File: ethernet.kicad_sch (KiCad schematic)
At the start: 1 part, among them U3 KSZ8081MLX

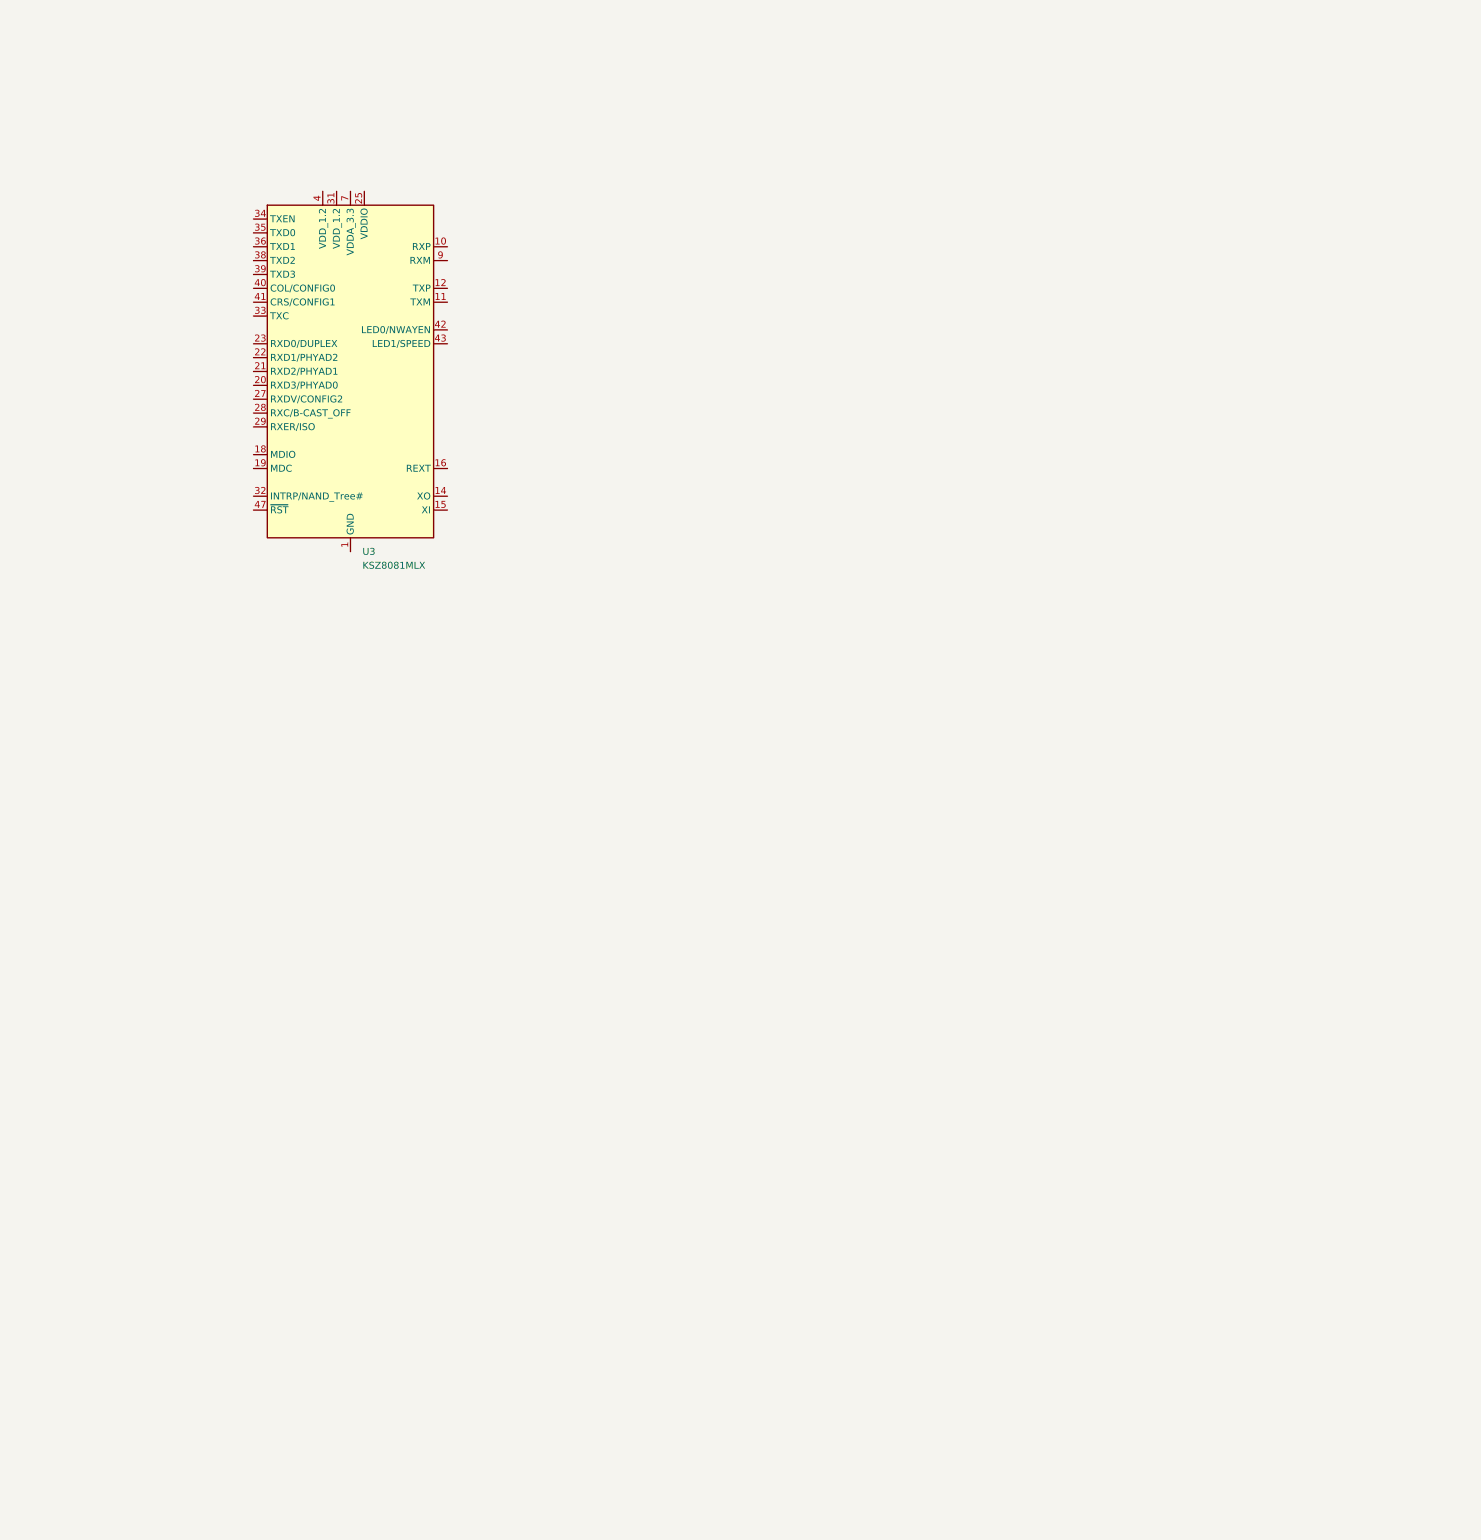
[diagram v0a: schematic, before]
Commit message: Working on ethernet schematic
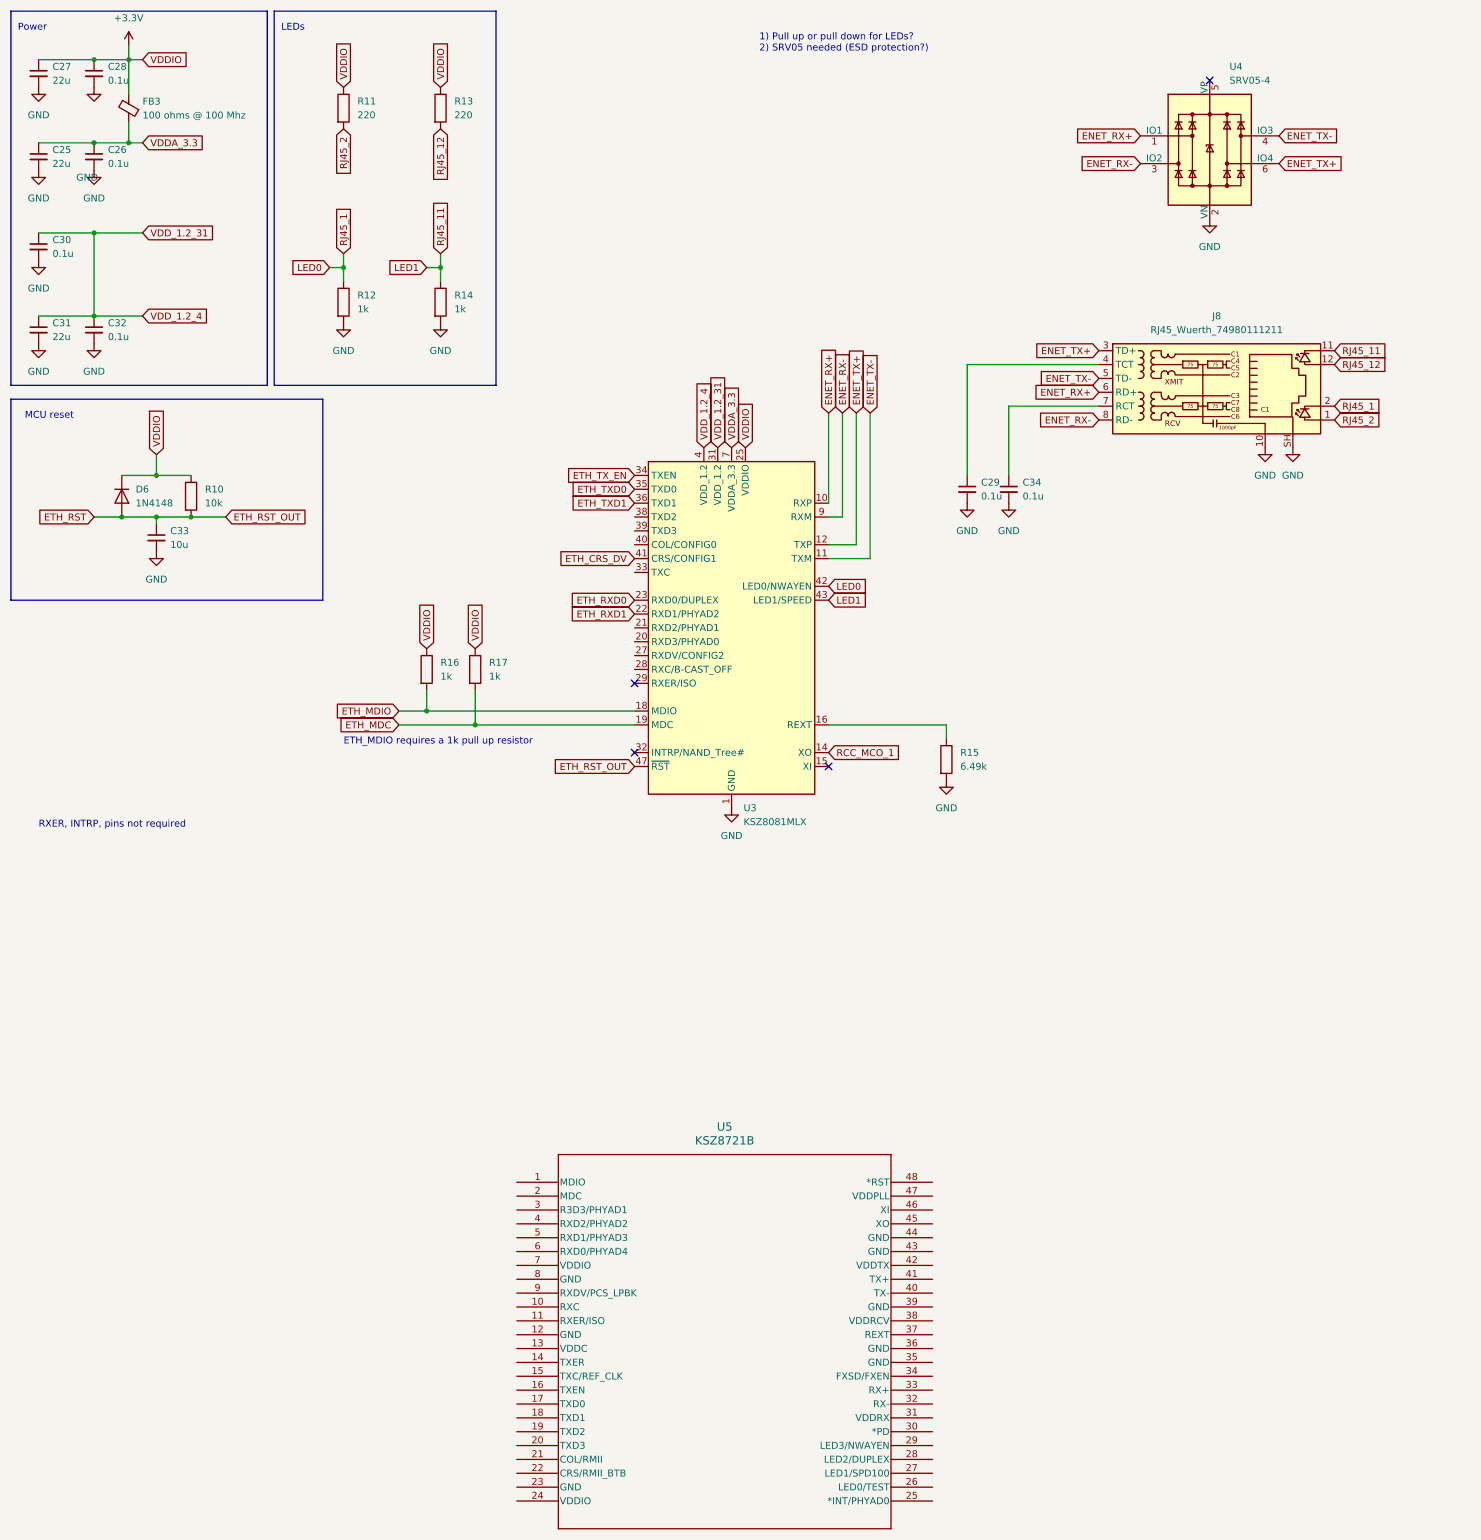
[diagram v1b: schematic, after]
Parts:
- added C25, C27, C31: 22u, symbol Device:C_Small
- added C26, C28, C29, C30, C32, C34: 0.1u, symbol Device:C_Small
- added C33: 10u, symbol Device:C_Small
- added D6: 1N4148, Diode_THT:D_DO-35_SOD27_P7.62mm_Horizontal, symbol Diode:1N4148
- added FB3: 100 ohms @ 100 Mhz, symbol Device:FerriteBead_Small
- added J8: RJ45_Wuerth_74980111211, Connector_RJ:RJ45_Wuerth_74980111211_Horizontal, symbol Connector:RJ45_Wuerth_74980111211
- added R10: 10k, symbol Device:R
- added R11, R13: 220, symbol Device:R
- added R12, R14, R16, R17: 1k, symbol Device:R
- added R15: 6.49k, symbol Device:R
- added U4: SRV05-4, Package_TO_SOT_SMD:SOT-23-6, symbol Power_Protection:SRV05-4
- added U5: KSZ8721B, SSOP48_15P875X7P493_MCH, symbol 2024-02-17_20-32-57:KSZ8721B
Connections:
- net GND: now reaches U3.1 (GND), U3.13 (GND), U3.17 (GND), U3.2 (GND), U3.24 (GND), U3.3 (GND), U3.30 (GND), U3.37 (GND)
- net GND: now also C25.2, C26.2, C27.2, C28.2, C29.2, C30.2, C31.2, C32.2, C33.2, C34.2, J8.10, J8.SH, R12.2, R14.2, R15.2, U4.2 (VN)
- net ENET_RX+: now reaches U3.10 (RXP)
- net ENET_RX+: now also J8.6 (RD+), U4.1 (IO1)
- net ENET_TX-: now reaches U3.11 (TXM)
- net ENET_TX-: now also J8.5 (TD-), U4.4 (IO3)
- net ENET_TX+: now reaches U3.12 (TXP)
- net ENET_TX+: now also J8.3 (TD+), U4.6 (IO4)
- net RCC_MCO_1: now reaches U3.14 (XO)
- net at U3.16 (REXT): now also R15.1
- net ETH_MDIO: now reaches U3.18 (MDIO)
- net ETH_MDIO: now also R16.2
- net ETH_MDC: now reaches U3.19 (MDC)
- net ETH_MDC: now also R17.2
- net ETH_RXD1: now reaches U3.22 (RXD1/PHYAD2)
- net ETH_RXD0: now reaches U3.23 (RXD0/DUPLEX)
- net +3.3V: now reaches U3.25 (VDDIO)
- net +3.3V: now also C27.1, C28.1, D6.1 (K), FB3.2, R10.1, R11.1, R13.1, R16.1, R17.1
- net VDD_1.2_31: now reaches U3.31 (VDD_1.2)
- net VDD_1.2_31: now also U3.4 (VDD_1.2), C30.1, C31.1, C32.1
- net ETH_TX_EN: now reaches U3.34 (TXEN)
- net ETH_TXD0: now reaches U3.35 (TXD0)
- net ETH_TXD1: now reaches U3.36 (TXD1)
- net ETH_CRS_DV: now reaches U3.41 (CRS/CONFIG1)
- net LED0: now reaches U3.42 (LED0/NWAYEN)
- net LED0: now also J8.2, R12.1
- net LED1: now reaches U3.43 (LED1/SPEED)
- net LED1: now also J8.11, R14.1
- net ETH_RST: now reaches U3.47 (~{RST})
- net ETH_RST: now also C33.1, D6.2 (A), R10.2
- net VDDA_3.3: now reaches U3.7 (VDDA_3.3)
- net VDDA_3.3: now also C25.1, C26.1, FB3.1
- net ENET_RX-: now reaches U3.9 (RXM)
- net ENET_RX-: now also J8.8 (RD-), U4.3 (IO2)
- new net: C29.1, J8.4 (TCT)
- new net: C34.1, J8.7 (RCT)
- new net RJ45_12: J8.12, R13.2
- new net RJ45_2: J8.1, R11.2
- no-connect marks 0 -> 4
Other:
- note added: "1) Pull up or pull down for LEDs? 2) SRV05 needed (ESD protection?)"
- note added: "ETH_MDIO requires a 1k pull up resistor"
- note added: "LEDs"
- note added: "MCU reset"
- note added: "Power"
- note added: "RXER, INTRP, pins not required"
- moved on the sheet: U3

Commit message: Redesign with KSZ8001L, but may need to use LAN8720 or LAN8740 if we want to use 25MHz clock signal
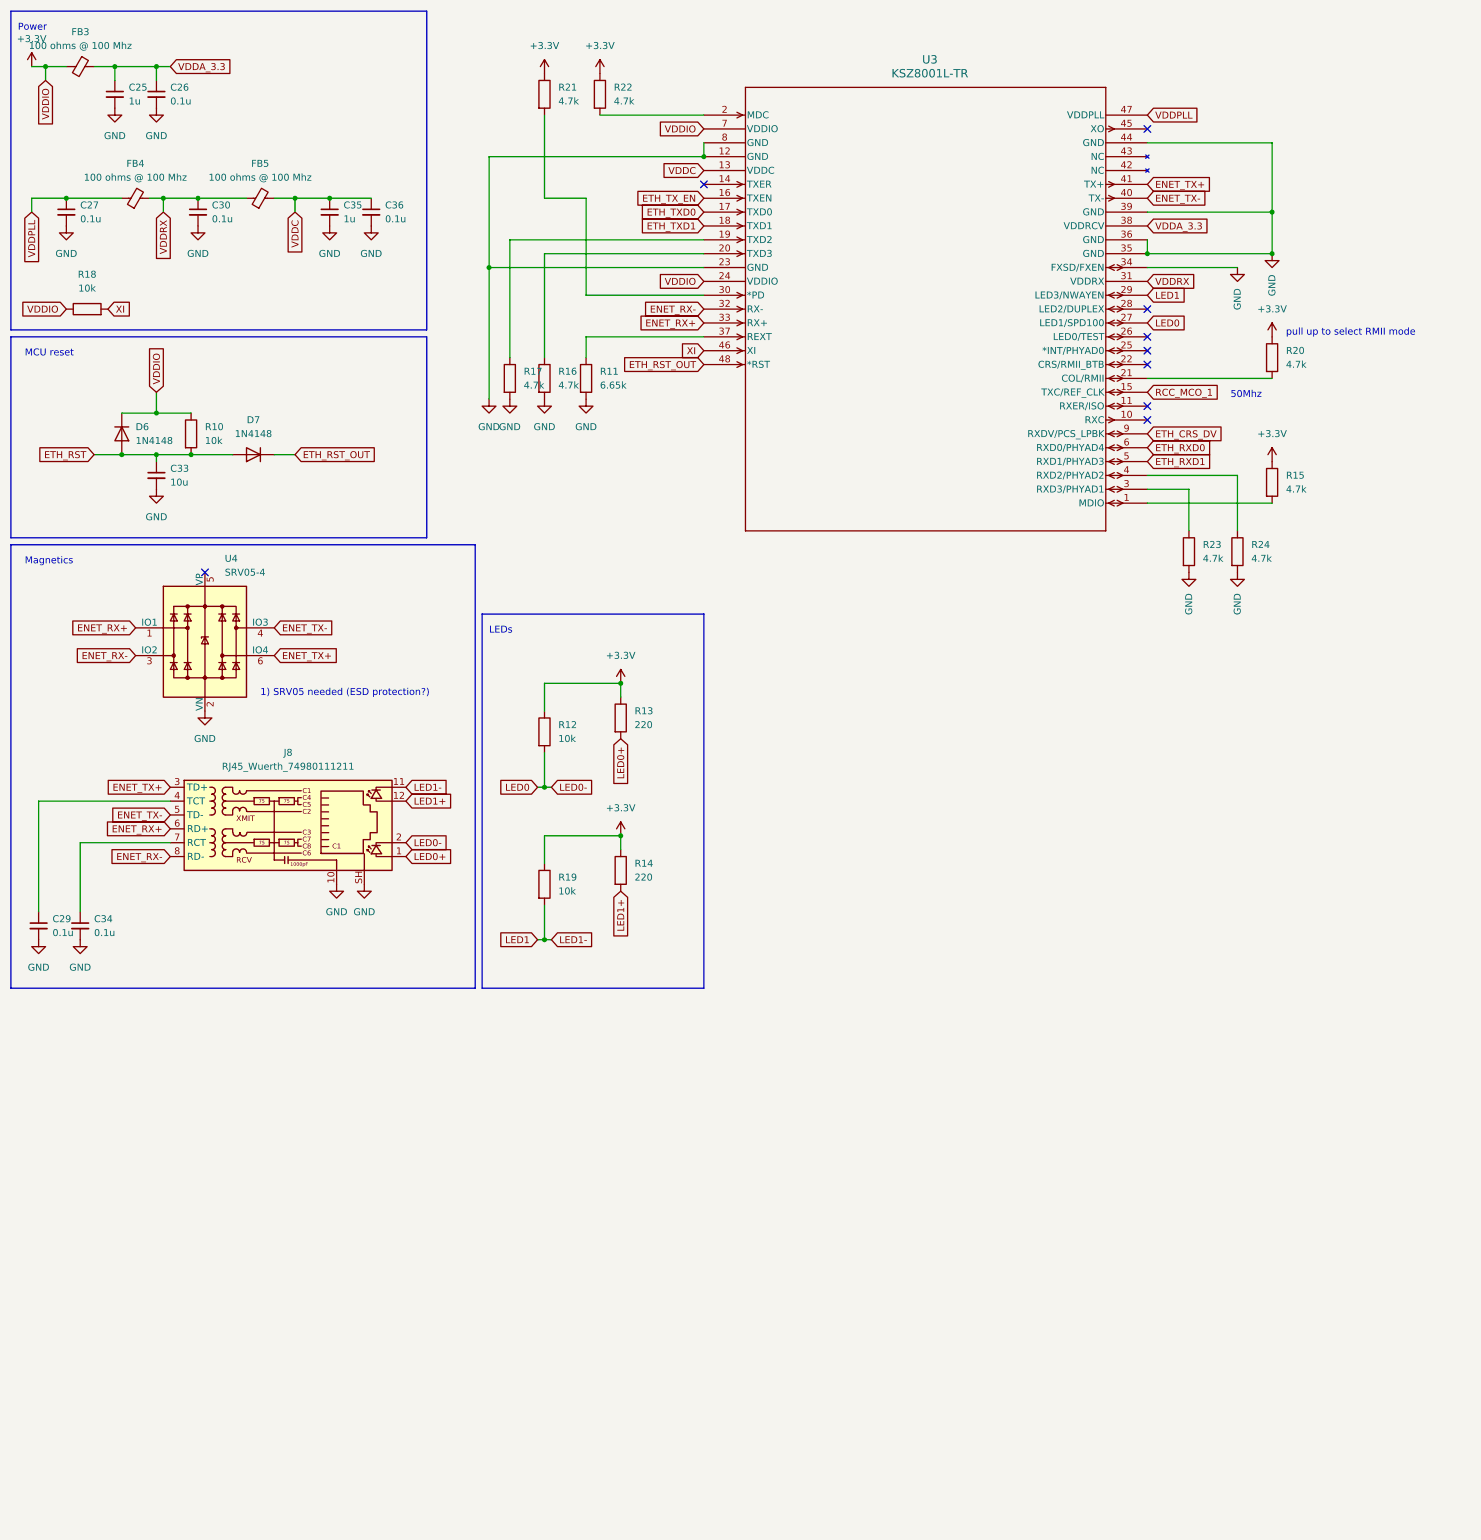
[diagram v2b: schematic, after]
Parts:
- removed C28, C32: 0.1u, symbol Device:C_Small
- removed C31: 22u, symbol Device:C_Small
- removed U3: KSZ8081MLX, Package_QFP:LQFP-48_7x7mm_P0.5mm, symbol Interface_Ethernet:KSZ8081MLX
- removed U5: KSZ8721B, SSOP48_15P875X7P493_MCH, symbol 2024-02-17_20-32-57:KSZ8721B
- added C35: 1u, symbol Device:C_Small
- added C36: 0.1u, symbol Device:C_Small
- added D7: 1N4148, Diode_THT:D_DO-35_SOD27_P7.62mm_Horizontal, symbol Diode:1N4148
- added FB4, FB5: 100 ohms @ 100 Mhz, symbol Device:FerriteBead_Small
- added R18, R19: 10k, symbol Device:R
- added R20, R21, R22, R23, R24: 4.7k, symbol Device:R
- added U3: KSZ8001L-TR, LQFP-48_MCH, symbol 2024-02-18_02-27-55:KSZ8001L-TR
- C25: value 22u -> 1u
- C27: value 22u -> 0.1u
- R11: value 220 -> 6.65k
- R12: value 1k -> 10k
- R14: value 1k -> 220
- R15: value 6.49k -> 4.7k
- R16, R17: value 1k -> 4.7k
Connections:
- net ETH_MDC is gone; now on net GND: R17.2
- net ETH_MDIO is gone; now on net GND: R16.2
- net +3.3V: now also R12.1, R14.1, R15.1, R18.1, R19.1, R20.1, R21.1, R22.1, U3.24 (VDDIO), U3.7 (VDDIO); no longer C27.1, R11.1, R16.1, R17.1
- net ENET_RX+: now also U3.33 (RX+)
- net ENET_RX-: now also U3.32 (RX-)
- net ENET_TX+: now also U3.41 (TX+)
- net ENET_TX-: now also U3.40 (TX-)
- net ETH_CRS_DV: now also U3.9 (RXDV/PCS_LPBK)
- net ETH_RST: now also D7.2 (A)
- net ETH_RXD0: now also U3.6 (RXD0/PHYAD4)
- net ETH_RXD1: now also U3.5 (RXD1/PHYAD3)
- net ETH_TXD0: now also U3.17 (TXD0)
- net ETH_TXD1: now also U3.18 (TXD1)
- net ETH_TX_EN: now also U3.16 (TXEN)
- net GND: now also R11.2, C35.2, C36.2, R23.2, R24.2, U3.12 (GND), U3.23 (GND), U3.34 (FXSD/FXEN), U3.35 (GND), U3.36 (GND), U3.39 (GND), U3.44 (GND), U3.8 (GND); no longer R12.2, R14.2, R15.2
- net LED0: now also R12.2, U3.27 (LED1/SPD100); no longer R12.1
- net LED1: now also R19.2, U3.29 (LED3/NWAYEN); no longer R14.1
- net RCC_MCO_1: now also U3.15 (TXC/REF_CLK)
- net VDDA_3.3: now also U3.38 (VDDRCV)
- net RJ45_12 renamed LED0+
- net LED0+: now also J8.1; no longer J8.12
- removed net RJ45_2: J8.1, R11.2
- net VDD_1.2_31 renamed VDDRX
- net VDDRX: now also FB4.2, FB5.1, U3.31 (VDDRX)
- new net: R15.2, U3.1 (MDIO)
- new net: R17.1, U3.19 (TXD2)
- new net: R11.1, U3.37 (REXT)
- new net: R22.2, U3.2 (MDC)
- new net: R23.1, U3.3 (RXD3/PHYAD1)
- new net: R21.2, U3.30 (*PD)
- new net: R16.1, U3.20 (TXD3)
- new net: R20.2, U3.21 (COL/RMII)
- new net: R24.1, U3.4 (RXD2/PHYAD2)
- new net ETH_RST_OUT: D7.1 (K), U3.48 (*RST)
- new net LED1+: J8.12, R14.2
- new net VDDC: C35.1, C36.1, FB5.2, U3.13 (VDDC)
- new net VDDPLL: C27.1, FB4.1, U3.47 (VDDPLL)
- new net XI: R18.2, U3.46 (XI)
- no-connect marks 4 -> 9
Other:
- note added: "1) SRV05 needed (ESD protection?)"
- note added: "50Mhz"
- note added: "Magnetics"
- note added: "pull up to select RMII mode"
- note removed: "1) Pull up or pull down for LEDs? 2) SRV05 needed (ESD protection?)"
- note removed: "ETH_MDIO requires a 1k pull up resistor"
- note removed: "RXER, INTRP, pins not required"
- moved on the sheet: C25, C26, C29, C33, C34, D6, FB3, J8, R10, U4
